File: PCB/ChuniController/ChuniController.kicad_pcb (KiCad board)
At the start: 2 copper layers, 4 parts

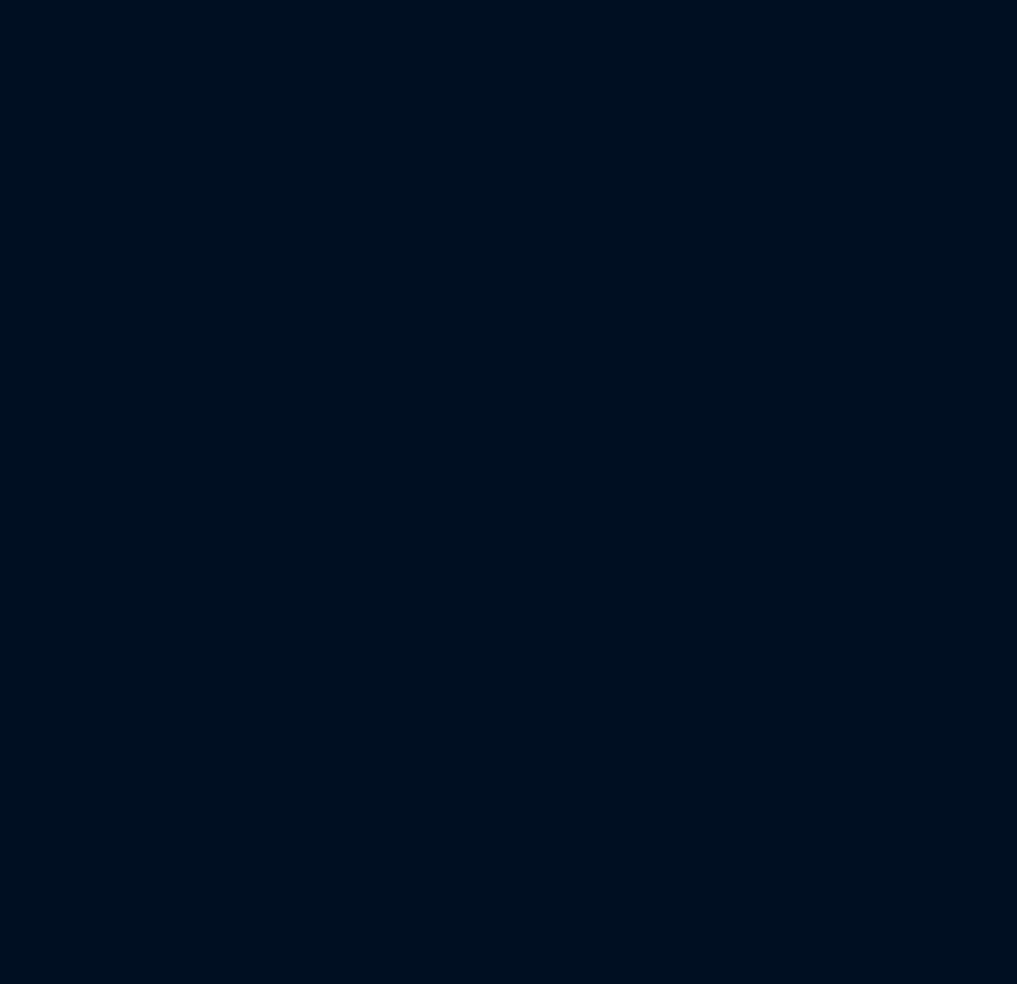
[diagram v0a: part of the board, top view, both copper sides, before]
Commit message: Add touch sensor
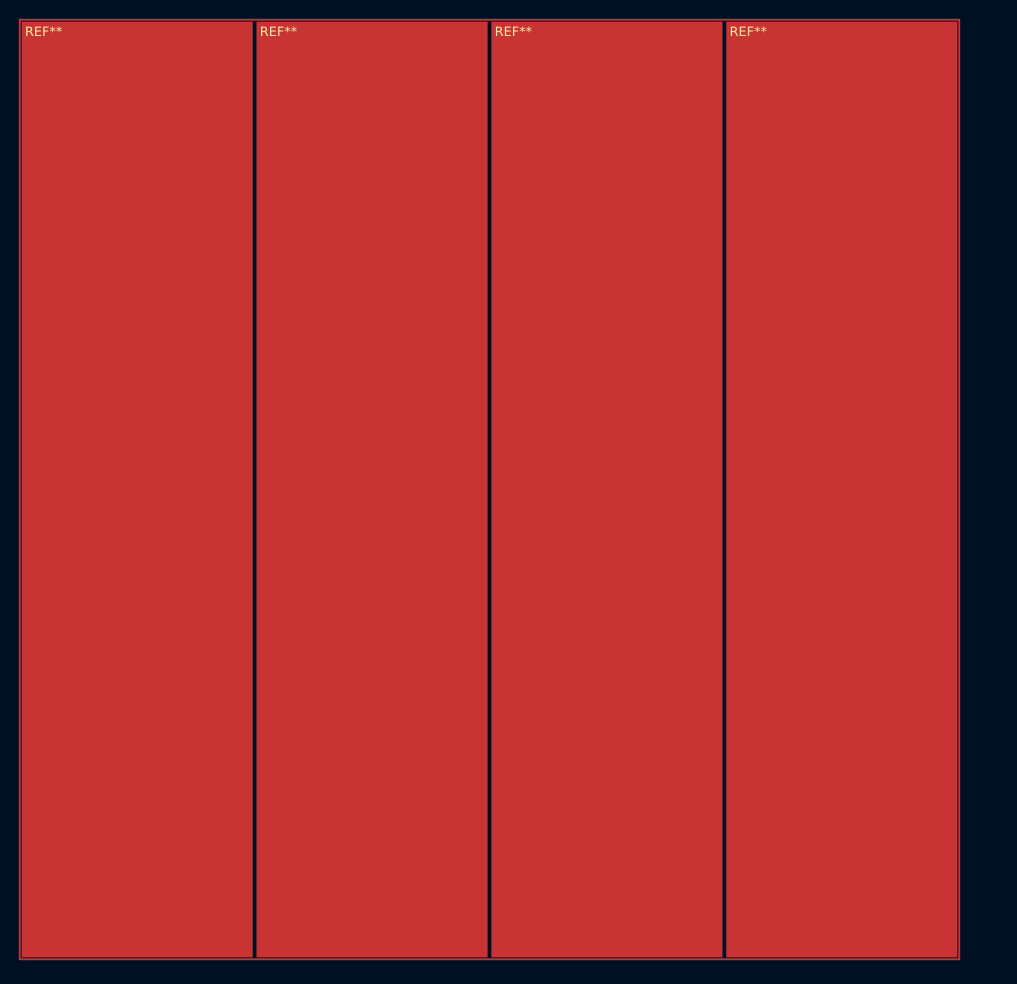
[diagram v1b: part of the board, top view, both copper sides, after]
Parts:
- added REF**: Slider_Pad, chuni_controller:Slider_Pad, F.Cu at (51.0, 49.5)
- added REF**: Slider_Pad, chuni_controller:Slider_Pad, F.Cu at (26.0, 49.5)
- added REF**: Slider_Pad, chuni_controller:Slider_Pad, F.Cu at (76.0, 49.5)
- added REF**: Slider_Pad, chuni_controller:Slider_Pad, F.Cu at (1.00, 49.5)

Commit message: PCB + CAD
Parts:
- added A1: RaspberryPi_Pico, Module:RaspberryPi_Pico_SMD, F.Cu at (238.1, 145.5)
- added D1: IR333C-A, LED_THT:LED_D5.0mm, F.Cu at (287.9, 155.3)
- added D2: IR333C-A, LED_THT:LED_D5.0mm, F.Cu at (259.4, 155.3)
- added D3: IR333C-A, LED_THT:LED_D5.0mm, F.Cu at (273.6, 169.2)
- added D4: IR333C-A, LED_THT:LED_D5.0mm, F.Cu at (278.1, 138.4)
- added D5: IR333C-A, LED_THT:LED_D5.0mm, F.Cu at (259.4, 169.2)
- added D6: IR333C-A, LED_THT:LED_D5.0mm, F.Cu at (273.6, 155.3)
- added Q1: Q_Photo_NPN, LED_THT:LED_D5.0mm, F.Cu at (250.0, 40.0)
- added Q10: AO3400, Package_TO_SOT_SMD:SOT-23, F.Cu at (278.1, 144.3)
- added Q11: AO3400, Package_TO_SOT_SMD:SOT-23, F.Cu at (259.4, 175.2)
- added Q12: AO3400, Package_TO_SOT_SMD:SOT-23, F.Cu at (273.6, 161.3)
- added Q2: Q_Photo_NPN, LED_THT:LED_D5.0mm, F.Cu at (285.0, 40.0)
- added Q3: Q_Photo_NPN, LED_THT:LED_D5.0mm, F.Cu at (320.0, 40.0)
- added Q4: Q_Photo_NPN, LED_THT:LED_D5.0mm, F.Cu at (355.0, 40.0)
- added Q5: Q_Photo_NPN, LED_THT:LED_D5.0mm, F.Cu at (390.0, 40.0)
- added Q6: Q_Photo_NPN, LED_THT:LED_D5.0mm, F.Cu at (425.0, 40.0)
- added Q7: AO3400, Package_TO_SOT_SMD:SOT-23, F.Cu at (287.9, 161.3)
- added Q8: AO3400, Package_TO_SOT_SMD:SOT-23, F.Cu at (259.4, 161.3)
- added Q9: AO3400, Package_TO_SOT_SMD:SOT-23, F.Cu at (273.6, 175.2)
- added R1: 1M, Resistor_SMD:R_0805_2012Metric_Pad1.20x1.40mm_HandSolder, F.Cu at (300.0, 40.0)
- added R10: 32R, Resistor_SMD:R_0805_2012Metric_Pad1.20x1.40mm_HandSolder, F.Cu at (283.0, 156.0)
- added R11: 100K, Resistor_SMD:R_0805_2012Metric_Pad1.20x1.40mm_HandSolder, F.Cu at (283.0, 158.9)
- added R12: 1K, Resistor_SMD:R_0805_2012Metric_Pad1.20x1.40mm_HandSolder, F.Cu at (254.6, 153.0)
- added R13: 32R, Resistor_SMD:R_0805_2012Metric_Pad1.20x1.40mm_HandSolder, F.Cu at (254.6, 156.0)
- added R14: 100K, Resistor_SMD:R_0805_2012Metric_Pad1.20x1.40mm_HandSolder, F.Cu at (254.6, 158.9)
- added R15: 1K, Resistor_SMD:R_0805_2012Metric_Pad1.20x1.40mm_HandSolder, F.Cu at (268.8, 167.0)
- added R16: 32R, Resistor_SMD:R_0805_2012Metric_Pad1.20x1.40mm_HandSolder, F.Cu at (268.8, 169.9)
- added R17: 100K, Resistor_SMD:R_0805_2012Metric_Pad1.20x1.40mm_HandSolder, F.Cu at (268.8, 172.9)
- added R18: 1K, Resistor_SMD:R_0805_2012Metric_Pad1.20x1.40mm_HandSolder, F.Cu at (273.3, 136.1)
- added R19: 32R, Resistor_SMD:R_0805_2012Metric_Pad1.20x1.40mm_HandSolder, F.Cu at (273.3, 139.1)
- added R2: 1M, Resistor_SMD:R_0805_2012Metric_Pad1.20x1.40mm_HandSolder, F.Cu at (305.0, 40.0)
- added R20: 100K, Resistor_SMD:R_0805_2012Metric_Pad1.20x1.40mm_HandSolder, F.Cu at (273.3, 142.0)
- added R21: 1K, Resistor_SMD:R_0805_2012Metric_Pad1.20x1.40mm_HandSolder, F.Cu at (254.6, 167.0)
- added R22: 32R, Resistor_SMD:R_0805_2012Metric_Pad1.20x1.40mm_HandSolder, F.Cu at (254.6, 169.9)
- added R23: 100K, Resistor_SMD:R_0805_2012Metric_Pad1.20x1.40mm_HandSolder, F.Cu at (254.6, 172.9)
- added R24: 1K, Resistor_SMD:R_0805_2012Metric_Pad1.20x1.40mm_HandSolder, F.Cu at (268.8, 153.0)
- added R25: 32R, Resistor_SMD:R_0805_2012Metric_Pad1.20x1.40mm_HandSolder, F.Cu at (268.8, 156.0)
- added R26: 100K, Resistor_SMD:R_0805_2012Metric_Pad1.20x1.40mm_HandSolder, F.Cu at (268.8, 158.9)
- added R3: 30k, Resistor_SMD:R_0805_2012Metric_Pad1.20x1.40mm_HandSolder, F.Cu at (261.0, 41.0)
- added R4: 30k, Resistor_SMD:R_0805_2012Metric_Pad1.20x1.40mm_HandSolder, F.Cu at (274.0, 41.0)
- added R5: 30k, Resistor_SMD:R_0805_2012Metric_Pad1.20x1.40mm_HandSolder, F.Cu at (331.0, 41.0)
- added R6: 30k, Resistor_SMD:R_0805_2012Metric_Pad1.20x1.40mm_HandSolder, F.Cu at (344.0, 41.0)
- added R7: 30k, Resistor_SMD:R_0805_2012Metric_Pad1.20x1.40mm_HandSolder, F.Cu at (401.0, 41.0)
- added R8: 30k, Resistor_SMD:R_0805_2012Metric_Pad1.20x1.40mm_HandSolder, F.Cu at (414.0, 41.0)
- added R9: 1K, Resistor_SMD:R_0805_2012Metric_Pad1.20x1.40mm_HandSolder, F.Cu at (283.0, 153.0)
- added U3: LM393D, LM393D:SOIC127P600X175-8N, F.Cu at (267.5, 40.0)
- added U4: LM393D, LM393D:SOIC127P600X175-8N, F.Cu at (407.5, 40.0)
- added U5: LM393D, LM393D:SOIC127P600X175-8N, F.Cu at (337.5, 40.0)
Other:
- board outline added: 186 x 10 mm

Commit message: PCB both ir board: ok add LM393D 3d model
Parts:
- added J4: Conn_01x04, Connector_JST:JST_SH_SM04B-SRSS-TB_1x04-1MP_P1.00mm_Horizontal, F.Cu at (229.0, 115.0)
- added J5: Conn_01x08, Connector_JST:JST_SH_SM08B-SRSS-TB_1x08-1MP_P1.00mm_Horizontal, F.Cu at (231.1, 41.1)
- added J6: Conn_01x08, Connector_JST:JST_SH_SM08B-SRSS-TB_1x08-1MP_P1.00mm_Horizontal, F.Cu at (231.0, 53.0)
- added J7: Conn_01x08, Connector_JST:JST_SH_SM08B-SRSS-TB_1x08-1MP_P1.00mm_Horizontal, F.Cu at (243.0, 40.0)
- added J8: Conn_01x08, Connector_JST:JST_SH_SM08B-SRSS-TB_1x08-1MP_P1.00mm_Horizontal, F.Cu at (243.0, 53.0)
- added R27: 10k, Resistor_SMD:R_0805_2012Metric_Pad1.20x1.40mm_HandSolder, F.Cu at (261.0, 38.0)
- added R28: 10k, Resistor_SMD:R_0805_2012Metric_Pad1.20x1.40mm_HandSolder, F.Cu at (331.0, 38.0)
- added R29: 10k, Resistor_SMD:R_0805_2012Metric_Pad1.20x1.40mm_HandSolder, F.Cu at (400.0, 38.0)
- added R30: 10k, Resistor_SMD:R_0805_2012Metric_Pad1.20x1.40mm_HandSolder, F.Cu at (277.0, 38.0)
- added R31: 10k, Resistor_SMD:R_0805_2012Metric_Pad1.20x1.40mm_HandSolder, F.Cu at (347.0, 38.0)
- added R32: 10k, Resistor_SMD:R_0805_2012Metric_Pad1.20x1.40mm_HandSolder, F.Cu at (417.0, 38.0)
- R10, R13, R16, R19, R22, R25: value 32R -> 50R
- R11, R14, R17, R20, R23, R26: value 100K -> 100k
- R12, R15, R18, R21, R24, R9: value 1K -> 1k
- moved R23 193.9 mm to (407.0, 53.0), turned to -90 degrees
- moved Q11 188.5 mm to (403.0, 53.0), turned to 180 degrees
- moved R22 186.4 mm to (398.1, 51.0)
- moved R26 184.5 mm to (420.0, 53.2), turned to -90 degrees
- moved D6 182.7 mm to (425.0, 53.0)
- moved R25 182.1 mm to (416.9, 50.0), turned to 180 degrees
- moved R21 182.0 mm to (398.1, 55.0)
- moved Q12 177.2 mm to (413.9, 53.0), turned to 90 degrees
- moved D5 174.8 mm to (390.0, 53.0)
- moved R24 173.0 mm to (409.9, 53.0), turned to 90 degrees
- moved R17 139.9 mm to (341.0, 53.0), turned to -90 degrees
- moved Q9 137.1 mm to (335.9, 53.0), turned to 180 degrees
- moved R20 135.9 mm to (376.0, 53.0), turned to -90 degrees
- moved R16 134.2 mm to (331.0, 51.0)
- moved Q10 130.2 mm to (370.9, 53.0), turned to 180 degrees
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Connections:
- A1 pad 10: /AirBlaster/SENSE2 -> /AirReceiver/SENSE2
- A1 pad 11: /AirBlaster/SENSE3 -> /AirReceiver/SENSE3
- A1 pad 12: /AirBlaster/SENSE4 -> /AirReceiver/SENSE4
- A1 pad 14: /AirBlaster/SENSE5 -> /AirReceiver/SENSE5
- A1 pad 15: /AirBlaster/SENSE6 -> /AirReceiver/SENSE6
- A1 pad 40: unconnected-(A1-VBUS-Pad40) -> +5V
- A1 pad 9: /AirBlaster/SENSE1 -> /AirReceiver/SENSE1
- D1 pad 2: +3V3 -> /AirBlaster/5V
- D2 pad 2: +3V3 -> /AirBlaster/5V
- D3 pad 2: +3V3 -> /AirBlaster/5V
- D4 pad 2: +3V3 -> /AirBlaster/5V
- D5 pad 2: +3V3 -> /AirBlaster/5V
- D6 pad 2: +3V3 -> /AirBlaster/5V
- Q10 pad 2: GND -> /AirBlaster/GND
- Q11 pad 2: GND -> /AirBlaster/GND
- Q12 pad 2: GND -> /AirBlaster/GND
- Q7 pad 2: GND -> /AirBlaster/GND
- Q8 pad 2: GND -> /AirBlaster/GND
- Q9 pad 2: GND -> /AirBlaster/GND
- R11 pad 1: GND -> /AirBlaster/GND
- R14 pad 1: GND -> /AirBlaster/GND
- R17 pad 1: GND -> /AirBlaster/GND
- R20 pad 1: GND -> /AirBlaster/GND
- R23 pad 1: GND -> /AirBlaster/GND
- R26 pad 1: GND -> /AirBlaster/GND
- U3 pad 1: /AirBlaster/SENSE1 -> /AirReceiver/SENSE1
- U3 pad 7: /AirBlaster/SENSE2 -> /AirReceiver/SENSE2
- U4 pad 1: /AirBlaster/SENSE1 -> /AirReceiver/SENSE3
- U4 pad 7: /AirBlaster/SENSE2 -> /AirReceiver/SENSE4
- U5 pad 1: /AirBlaster/SENSE1 -> /AirReceiver/SENSE5
- U5 pad 7: /AirBlaster/SENSE2 -> /AirReceiver/SENSE6
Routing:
- net +3V3: track 0.00 -> 229.0 mm
- net /AirBlaster/5V: track 0.00 -> 214.8 mm
- net /AirReceiver/IRReceiver/COMP_IN: track 0.00 -> 187.0 mm, vias 0 -> 7
- net /AirReceiver/SENSE5: track 0.00 -> 177.0 mm
- net /AirReceiver/SENSE6: track 0.00 -> 176.6 mm
- net /AirBlaster/EMIT6: track 0.00 -> 167.2 mm
- net /AirBlaster/EMIT5: track 0.00 -> 155.1 mm
- net /AirBlaster/EMIT4: track 0.00 -> 122.0 mm
- net /AirReceiver/SENSE4: track 0.00 -> 106.2 mm
- net /AirReceiver/SENSE3: track 0.00 -> 105.0 mm
- net /AirBlaster/EMIT3: track 0.00 -> 87.1 mm
- net /AirBlaster/GND: track 0.00 -> 53.7 mm, vias 0 -> 7
- net /AirBlaster/EMIT2: track 0.00 -> 52.2 mm
- net /AirReceiver/SENSE2: track 0.00 -> 35.9 mm
- net /AirReceiver/SENSE1: track 0.00 -> 35.7 mm
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- added copper zone on B.Cu, net /AirBlaster/GND
- added copper zone on B.Cu, net GND
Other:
- board size 186 x 10 mm -> 192 x 25 mm

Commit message: PCB
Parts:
- moved A1 124.6 mm to (353.6, 98.9), turned to 90 degrees
- moved J6 18.6 mm to (225.9, 70.9), turned to 0 degrees
- moved J5 14.2 mm to (220.0, 50.0), turned to 0 degrees
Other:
- board size 192 x 25 mm -> 192 x 81 mm
